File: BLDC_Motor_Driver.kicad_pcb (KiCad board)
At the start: 2 copper layers, 147.2 x 104.8 mm, 98 parts, among them IC1 AS5047P-ATSM, IC2 L6498D, IC3 ATSAMD21G18A-MFT, IC4 AD8030ARZ, IC5 LTC6655BHMS8-1.25#TRPBF, IC6 L6498D, IC7 L6498D, IC8 TPS7A4901DGNT, IC9 AD8030ARZ, J1 FTSH-105-01-L-DV-K, J2 031-5431-10RFX, J3 031-5431-10RFX, J4 031-5431-10RFX, J5 031-5431-10RFX, J6 Conn_01x06_Pin, Q1 IPB320N20N3GATMA1, Q2 IPB320N20N3GATMA1, Q3 IPB320N20N3GATMA1, Q4 IPB320N20N3GATMA1, Q5 IPB320N20N3GATMA1, Q6 IPB320N20N3GATMA1

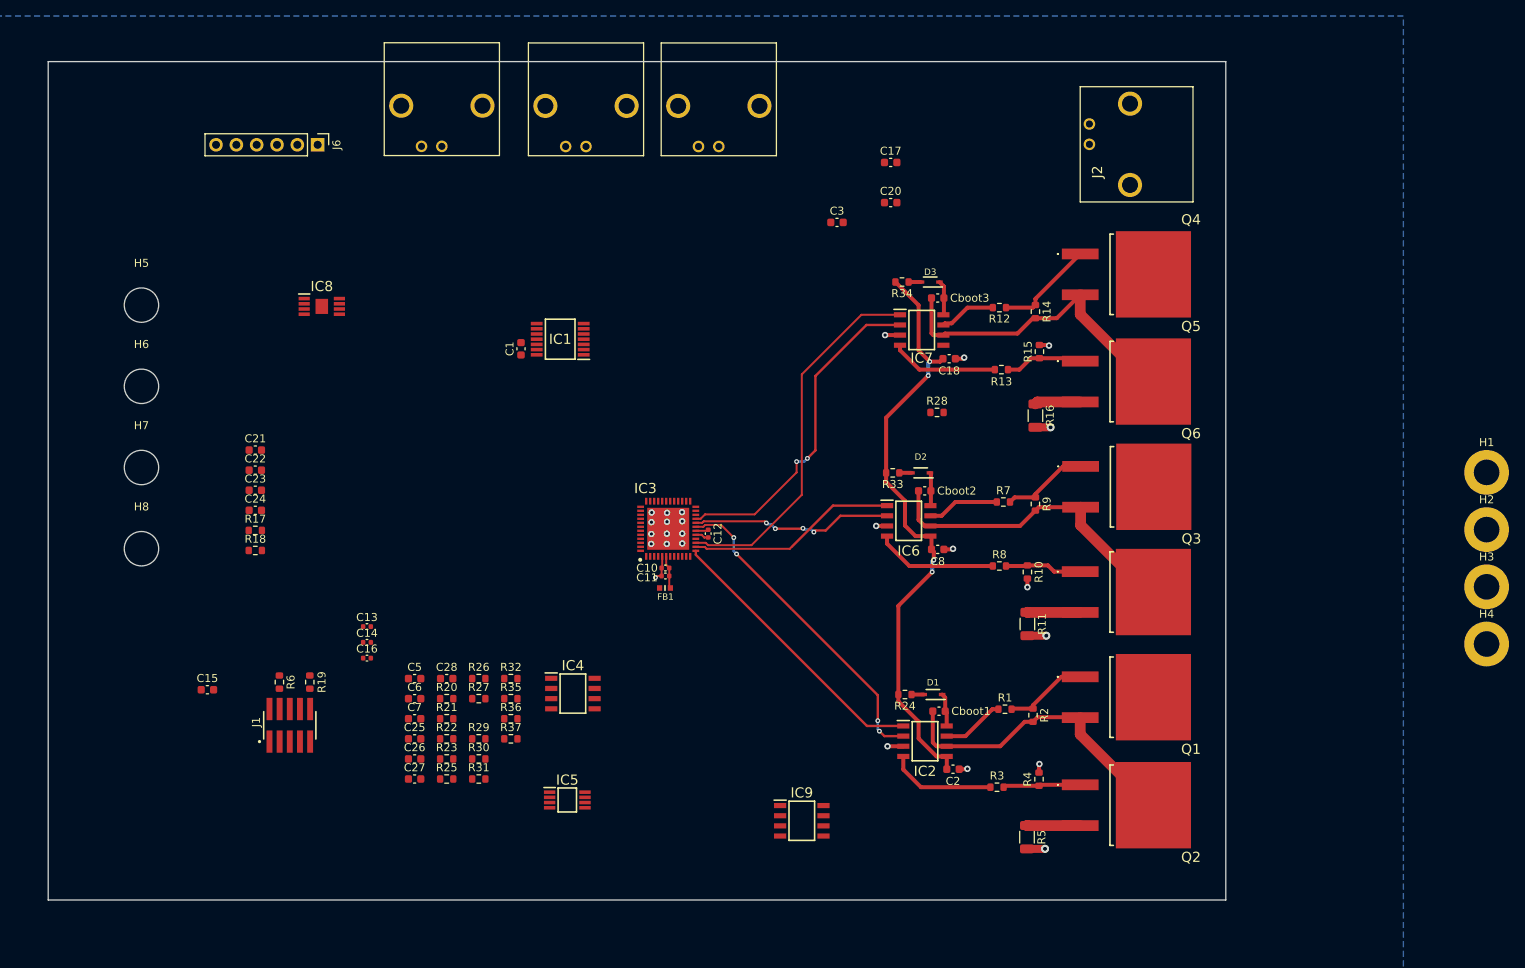
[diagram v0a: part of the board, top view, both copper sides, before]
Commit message: Almost all routing done
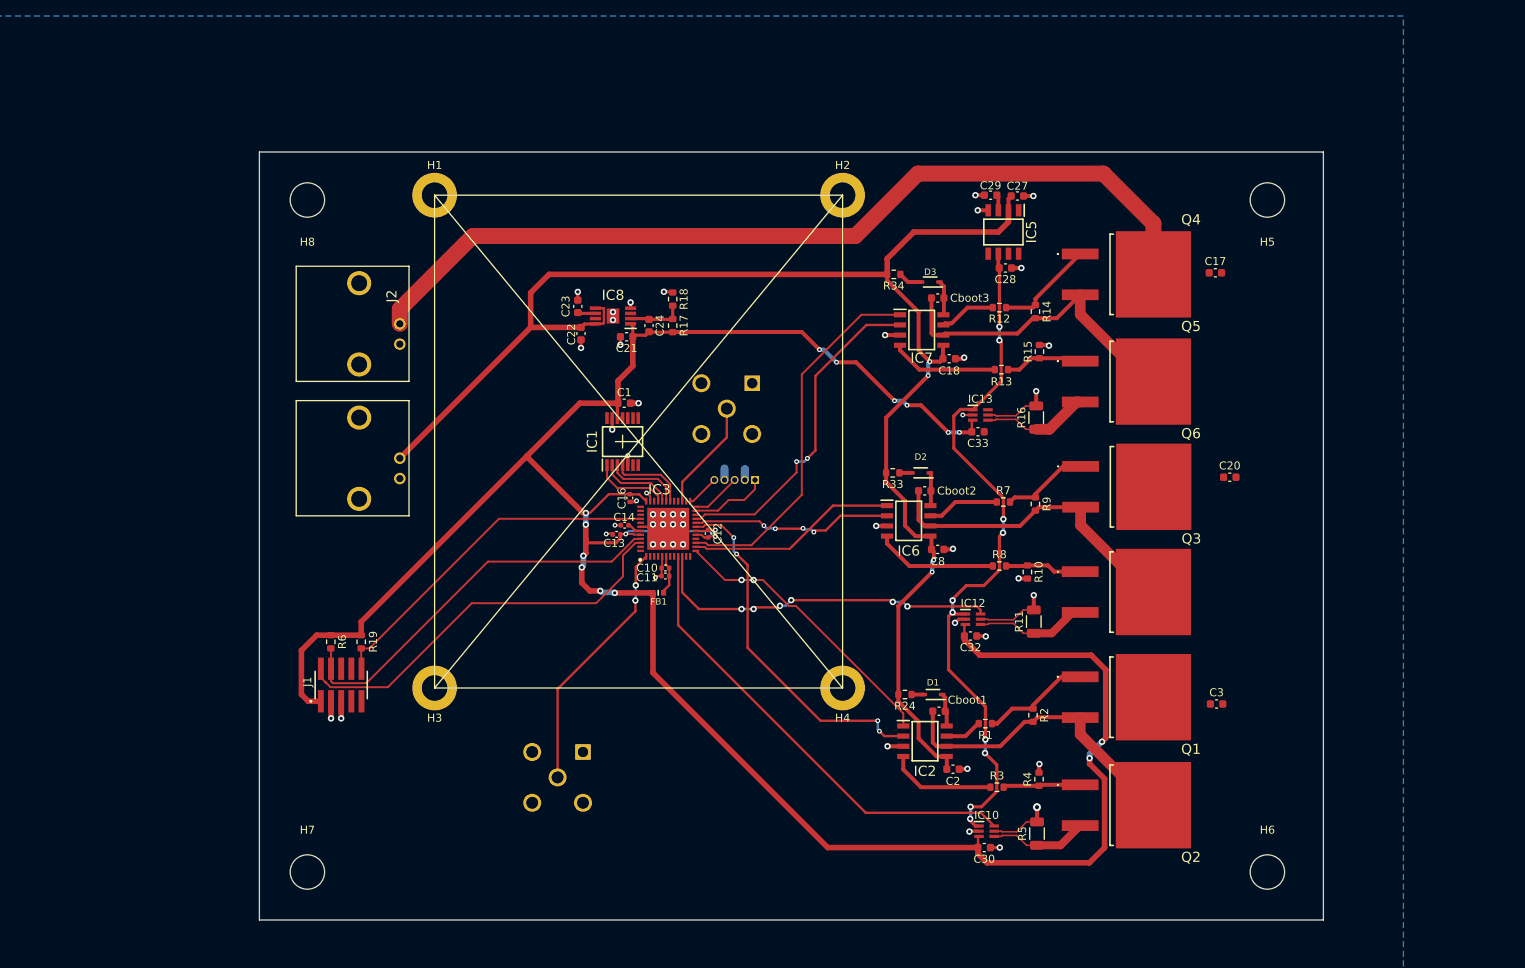
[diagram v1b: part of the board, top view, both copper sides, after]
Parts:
- removed C15: 10u, Capacitor_SMD:C_0603_1608Metric
- removed C25, C6, C7: TBD, Capacitor_SMD:C_0603_1608Metric
- removed C26, C5: 0.1u, Capacitor_SMD:C_0603_1608Metric
- removed IC4, IC9: AD8030ARZ, BLDC-Motor-Driver:AD8030ARZ-SOIC8
- removed J6: Conn_01x06_Pin, Connector_PinHeader_2.54mm:PinHeader_1x06_P2.54mm_Vertical
- removed R20, R21, R22, R23, R25, R26, R27, R28, R29, R30, R31, R32, R35, R36, R37: 10k, Resistor_SMD:R_0603_1608Metric
- added C29: 10nF, Capacitor_SMD:C_0603_1608Metric, F.Cu at (168.4, 42.4)
- added C30: 0.1u, Capacitor_SMD:C_0603_1608Metric, F.Cu at (167.6, 123.9)
- added C32: 0.1u, Capacitor_SMD:C_0603_1608Metric, F.Cu at (165.9, 97.5)
- added C33: 0.1u, Capacitor_SMD:C_0603_1608Metric, F.Cu at (166.8, 72.0)
- added IC10: INA214AIDCKT, BLDC-Motor-Driver:INA214AIDCKT, F.Cu at (167.9, 121.9)
- added IC12: INA214AIDCKT, BLDC-Motor-Driver:INA214AIDCKT, F.Cu at (166.2, 95.4)
- added IC13: INA214AIDCKT, BLDC-Motor-Driver:INA214AIDCKT, F.Cu at (167.1, 69.9)
- added J7: 112405-12, BLDC-Motor-Driver:11240512, B.Cu at (138.6, 65.9)
- added NT1: NetTie_2, NetTie:NetTie-2_SMD_Pad0.5mm, F.Cu at (173.8, 92.9)
- added NT2: NetTie_2, NetTie:NetTie-2_SMD_Pad0.5mm, F.Cu at (174.2, 119.4)
- added NT3: NetTie_2, NetTie:NetTie-2_SMD_Pad0.5mm, F.Cu at (174.1, 67.4)
- IC5: value LTC6655BHMS8-1.25#TRPBF -> ISL21090BFB812Z-TK; footprint BLDC-Motor-Driver:LTC6655 -> BLDC-Motor-Driver:ISL21090
- J4: value 031-5431-10RFX -> 112405-12; footprint BLDC-Motor-Driver:031543110RFX -> BLDC-Motor-Driver:11240512; moved to B.Cu
- J5: value 031-5431-10RFX -> Conn_01x05_Pin; footprint BLDC-Motor-Driver:031543110RFX -> Connector_PinHeader_1.27mm:PinHeader_1x05_P1.27mm_Vertical; moved to B.Cu
- moved H6 153.3 mm to (203.0, 127.0)
- moved H5 141.4 mm to (203.0, 43.0), turned to 180 degrees
- moved H1 136.0 mm to (98.9, 42.4)
- moved H3 132.1 mm to (98.9, 104.0), turned to 180 degrees
- moved C27 104.8 mm to (171.8, 42.5), turned to 180 degrees
- moved H2 90.7 mm to (149.9, 42.4)
- moved J2 90.5 mm to (94.6, 61.0), turned to 90 degrees
- moved IC5 89.5 mm to (170.0, 47.0), turned to -90 degrees
- moved C28 86.7 mm to (170.2, 51.5), turned to 180 degrees
- moved H4 80.7 mm to (149.9, 104.0), turned to 180 degrees
- moved C3 76.7 mm to (196.7, 106.0)
- moved J4 75.7 mm to (117.5, 112.0), turned to 180 degrees
- moved R18 60.9 mm to (128.7, 55.4), turned to 90 degrees
- moved R17 58.1 mm to (128.7, 58.7), turned to 90 degrees
- moved H7 54.6 mm to (83.0, 127.0)
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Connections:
- C27 pad 2: +3V3 -> +12V
- IC3 pad 1: unconnected-(IC3-PA00-Pad1) -> /Microcontroller/SERCOM1_PAD0
- IC3 pad 22: /Microcontroller/SERCOM4_PAD1 -> unconnected-(IC3-PA13-Pad22)
- IC3 pad 23: /Microcontroller/SERCOM4_PAD2 -> /Microcontroller/BENCHMARK_IO_1
- IC3 pad 24: unconnected-(IC3-PA15-Pad24) -> /Microcontroller/BENCHMARK_IO_2
- IC3 pad 25: unconnected-(IC3-PA16-Pad25) -> /Microcontroller/BENCHMARK_IO_3
- IC3 pad 26: /Microcontroller/SERCOM3_PAD1 -> unconnected-(IC3-PA17-Pad26)
- IC3 pad 37: /Microcontroller/BENCHMARK_IO_1 -> unconnected-(IC3-PB22-Pad37)
- IC3 pad 38: /Microcontroller/BENCHMARK_IO_2 -> unconnected-(IC3-PB23-Pad38)
- IC3 pad 39: /Microcontroller/BENCHMARK_IO_3 -> unconnected-(IC3-PA27-Pad39)
- IC5 pad 1: Net-(IC5-~{SHDN}) -> unconnected-(IC5-DNC_1-Pad1)
- IC5 pad 2: +3V3 -> +12V
- IC5 pad 3: GND -> Net-(IC5-COMP)
- IC5 pad 5: GND -> unconnected-(IC5-TRIM-Pad5)
- IC5 pad 7: /Current Sensing Difference Amplifier/VREF -> unconnected-(IC5-DNC_2-Pad7)
- IC5 pad 8: GND -> unconnected-(IC5-DNC_3-Pad8)
- J1 pad 01: +3.3V -> +3V3
- J3 pad 1: +12V -> GND
- J3 pad 2: GND -> +12V
- J4 pad 1: GND -> unconnected-(J4-Pad1)
- J4 pad 2: /Microcontroller/SERCOM3_PAD2 -> unconnected-(J4-Pad2)
- J4 pad 4: unconnected-(J4-Pad4) -> GND
- J5 pad 1: GND -> /Microcontroller/BENCHMARK_IO_1
- J5 pad 2: /Microcontroller/SERCOM4_PAD2 -> GND
- J5 pad 3: unconnected-(J5-Pad3) -> /Microcontroller/BENCHMARK_IO_2
- J5 pad 4: unconnected-(J5-Pad4) -> GND
- R11 pad 2: GND -> /Current Sensing Difference Amplifier/CSA_PH_B_IN-
- R16 pad 2: GND -> /Current Sensing Difference Amplifier/CSA_PH_C_IN-
- R5 pad 2: GND -> /Current Sensing Difference Amplifier/CSA_PH_A_IN-
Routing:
- net +3V3: track 1.69 -> 307.9 mm, vias 0 -> 16
- net VBUS: track 0.00 -> 112.0 mm
- net +12V: track 75.4 -> 186.1 mm
- net /Current Sensing Difference Amplifier/VREF: track 0.00 -> 88.9 mm, vias 0 -> 10
- net /Current Sensing Difference Amplifier/CSA_PH_A_VOUT: track 0.00 -> 58.5 mm
- net /Microcontroller/SWDIO: track 0.00 -> 50.6 mm
- net /Microcontroller/SWCLK: track 0.00 -> 50.4 mm
- net /Microcontroller/RESET: track 0.00 -> 44.2 mm
- net /Current Sensing Difference Amplifier/CSA_PH_B_VOUT: track 0.00 -> 44.1 mm, vias 0 -> 6
- net /Microcontroller/SERCOM1_PAD0: track 0.00 -> 32.2 mm, vias 0 -> 2
- net GND: track 23.4 -> 50.0 mm, vias 25 -> 51
- net /Microcontroller/SERCOM3_PAD2: track 0.00 -> 13.9 mm
- net /Microcontroller/BENCHMARK_IO_1: track 0.00 -> 9.67 mm
- net /Microcontroller/SERCOM5_PAD3: track 0.00 -> 9.64 mm
- net /Microcontroller/SERCOM5_PAD0: track 0.00 -> 9.57 mm
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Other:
- board size 147.2 x 104.8 mm -> 133 x 96 mm

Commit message: More routing
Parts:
- J4, J7: moved to F.Cu
- moved J7 59.1 mm to (117.0, 120.9), turned to 0 degrees
- moved J4 18.6 mm to (101.1, 120.9), turned to 0 degrees
- moved J1 10.8 mm to (88.1, 92.9)
- moved R19 10.8 mm to (90.6, 87.5)
- moved R6 10.8 mm to (86.8, 87.5)
- moved R34 4.43 mm to (160.2, 50.2)
- moved R33 3.13 mm to (157.9, 74.5)
- moved R24 2.71 mm to (159.1, 102.5)
- moved C33 1.26 mm to (165.8, 72.7), turned to 90 degrees
- moved D3 0.98 mm to (161.8, 53.0)
- moved D2 0.54 mm to (160.2, 77.1)
- moved D1 0.52 mm to (161.6, 104.5)
- moved C10 0.25 mm to (127.5, 89.0)
- moved C11 0.25 mm to (127.5, 90.0)
- moved Cboot1 0.25 mm to (162.2, 106.9)
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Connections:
- IC3 pad 27: /Microcontroller/SERCOM3_PAD2 -> unconnected-(IC3-PA18-Pad27)
- IC3 pad 7: unconnected-(IC3-PB08-Pad7) -> /Microcontroller/SERCOM4_PAD0
- J7 pad 5: /Microcontroller/SERCOM3_PAD2 -> /Microcontroller/SERCOM4_PAD0
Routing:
- net /Current Sensing Difference Amplifier/CSA_PH_C_VOUT: track 0.00 -> 66.0 mm, vias 0 -> 4
- net /Microcontroller/SERCOM4_PAD0: track 0.00 -> 40.2 mm, vias 0 -> 2
- net /Microcontroller/SERCOM3_PAD2: track 13.9 -> 0.00 mm
- net /Microcontroller/SERCOM1_PAD0: track 32.2 -> 45.3 mm
- net +3V3: track 307.9 -> 301.4 mm
- net /Microcontroller/SWDIO: track 50.6 -> 45.3 mm
- net /Microcontroller/SWCLK: track 50.4 -> 45.1 mm
- net /Microcontroller/RESET: track 44.2 -> 38.9 mm
- net /Microcontroller/TCC0_WO6: track 41.8 -> 47.1 mm, vias 2 -> 0
- net /Microcontroller/TCC0_WO5: track 25.4 -> 29.8 mm, vias 4 -> 0
- net /Microcontroller/TCC0_WO2: track 46.4 -> 48.4 mm, vias 0 -> 2
- net /Microcontroller/TCC0_WO0: track 35.9 -> 37.8 mm
- net +12V: track 186.1 -> 184.7 mm, vias 4 -> 6
- net Net-(D2-A): track 1.53 -> 2.96 mm
- net GND: track 50.0 -> 51.2 mm, vias 51 -> 72
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
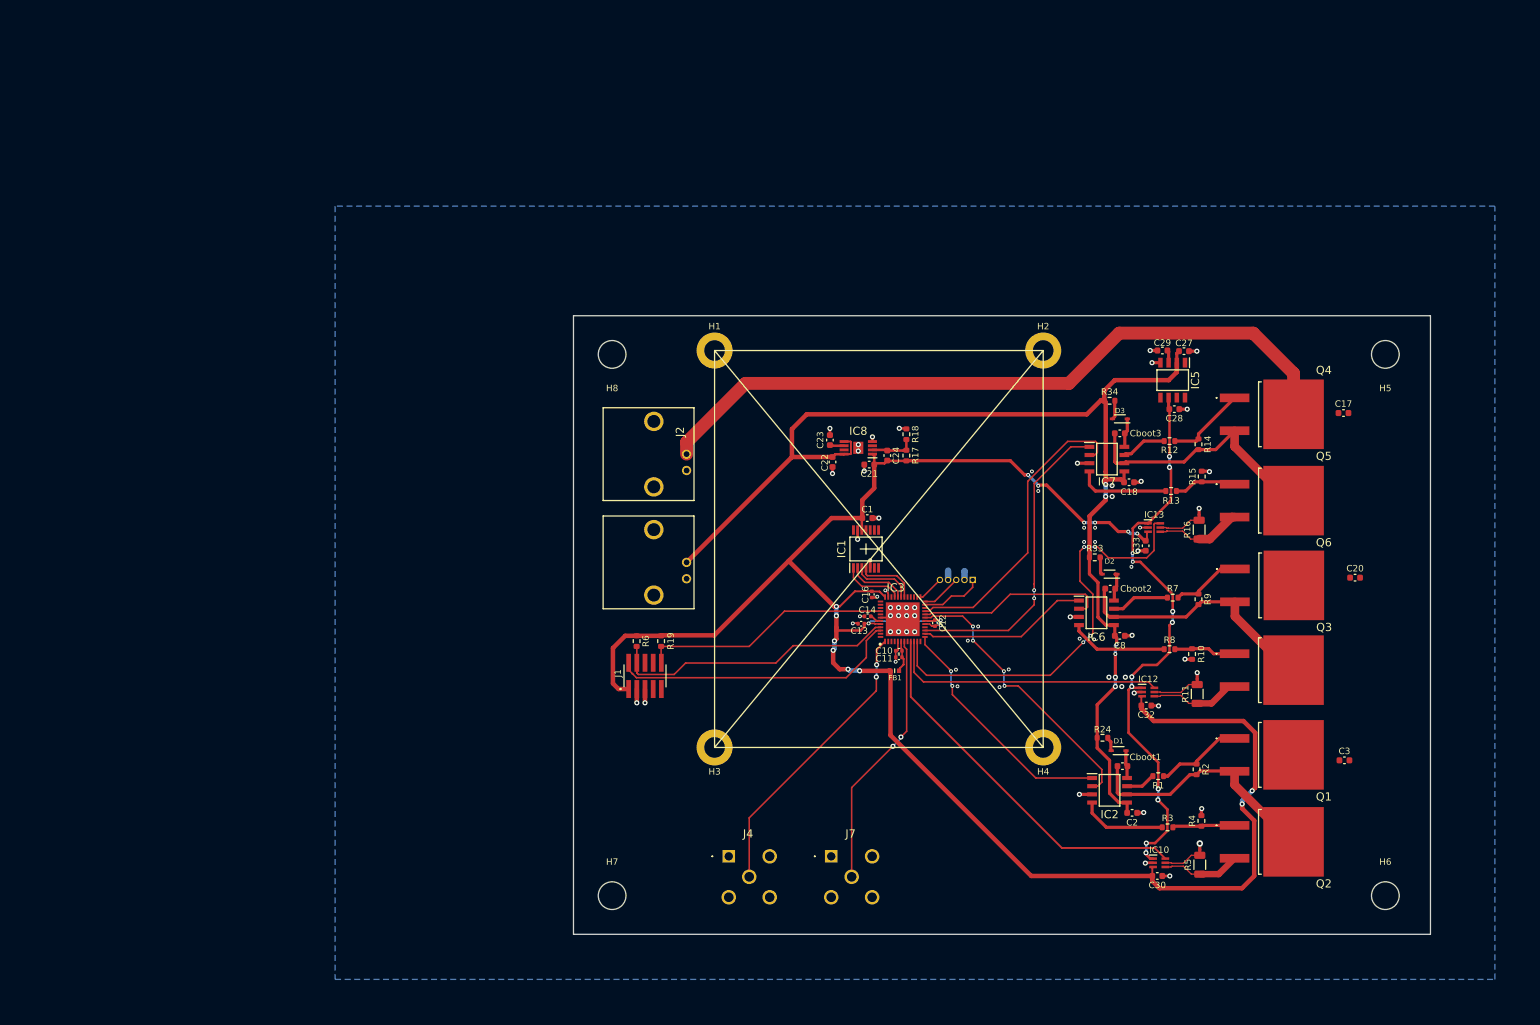
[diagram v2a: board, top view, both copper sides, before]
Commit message: Add capacitors
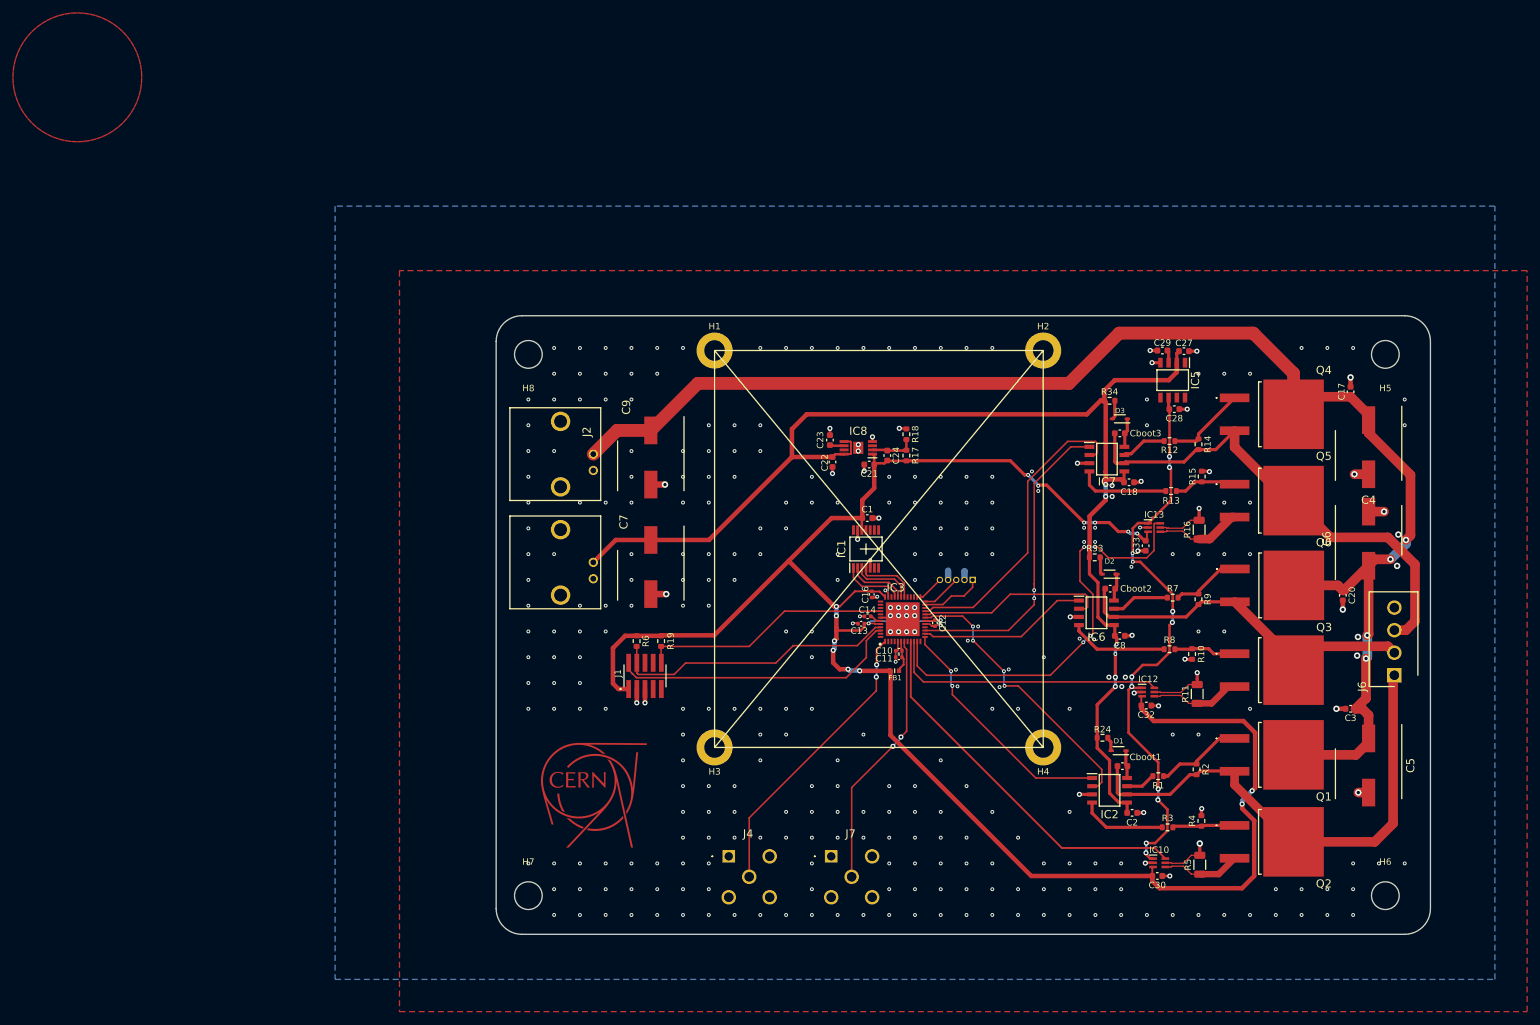
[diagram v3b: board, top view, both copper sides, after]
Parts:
- added C4: 220uF, BLDC-Motor-Driver:CAPAE1030X1050N, F.Cu at (200.4, 57.4)
- added C5: 220uF, BLDC-Motor-Driver:CAPAE1030X1050N, F.Cu at (200.4, 106.8)
- added C6: 220uF, BLDC-Motor-Driver:CAPAE1030X1050N, F.Cu at (200.4, 71.6)
- added C7: 220uF, BLDC-Motor-Driver:CAPAE1030X1050N, F.Cu at (89.0, 76.0)
- added C9: 220uF, BLDC-Motor-Driver:CAPAE1030X1050N, F.Cu at (89.0, 59.0)
- added G***: LOGO, BLDC-Motor-Driver:cern_logo, F.Cu at (80.2, 111.4)
- added J6: Conn_01x04_Socket, BLDC-Motor-Driver:SHDR4W91P0X350_1X4_1400X730X875P, F.Cu at (204.4, 92.8)
- moved J2 14.5 mm to (80.1, 61.0)
- moved J3 14.5 mm to (80.1, 77.8)
- moved H7 13.0 mm to (70.0, 127.0)
- moved H8 13.0 mm to (70.0, 43.0)
- moved C3 8.06 mm to (197.6, 98.0), turned to 180 degrees
- moved C17 3.48 mm to (197.6, 48.8), turned to 90 degrees
- moved C20 3.34 mm to (196.4, 80.4), turned to -90 degrees
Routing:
- net VBUS: track 112.0 -> 225.2 mm, vias 0 -> 4
- net /Power Stage - Inverter & Gate Drivers/OUT_PHASE_A: track 38.9 -> 78.6 mm
- net /Power Stage - Inverter & Gate Drivers/OUT_PHASE_C: track 40.3 -> 75.9 mm
- net /Power Stage - Inverter & Gate Drivers/OUT_PHASE_B: track 40.0 -> 57.2 mm
- net GND: track 51.2 -> 66.3 mm, vias 72 -> 342
- net +12V: track 184.7 -> 199.1 mm
- added copper zone on F.Cu, net (none)
- added copper zone on F.Cu, net GND
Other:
- board size 133 x 96 mm -> 145 x 96 mm
